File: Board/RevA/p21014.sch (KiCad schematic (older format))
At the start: 1 part

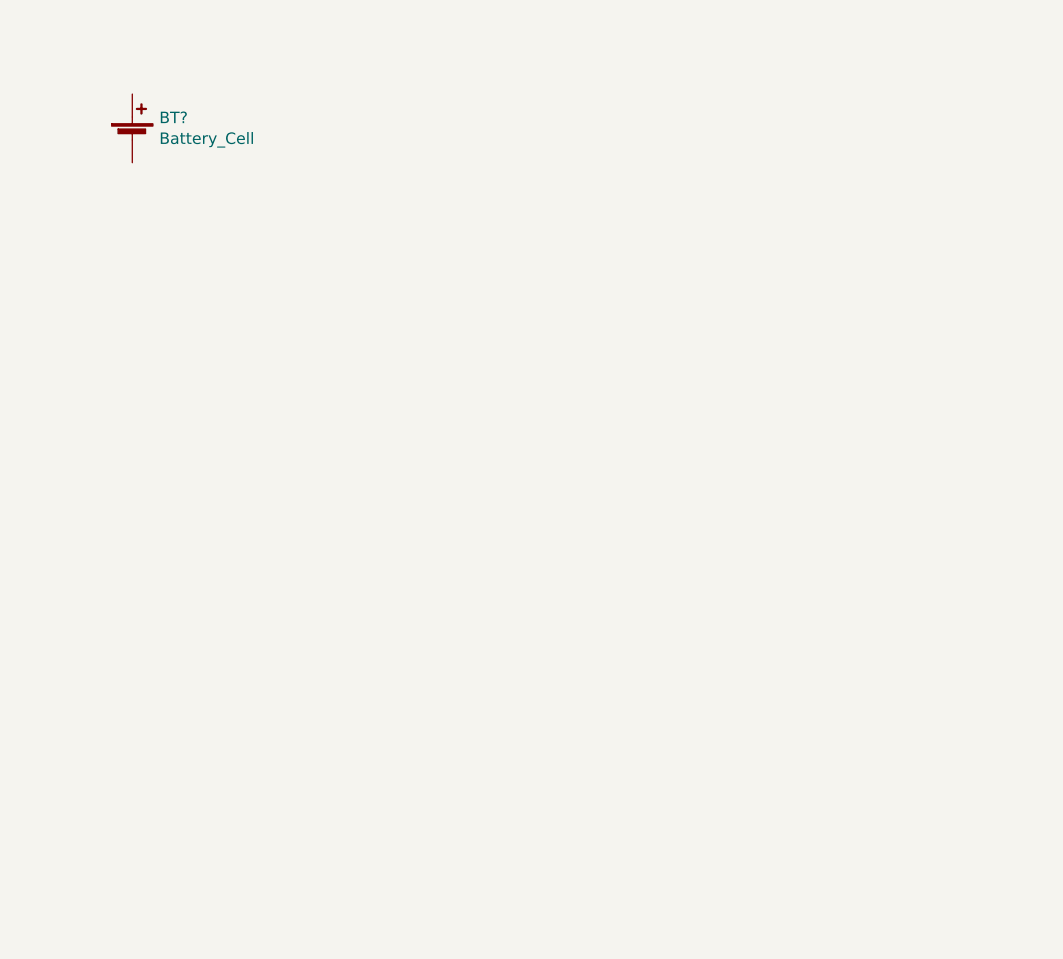
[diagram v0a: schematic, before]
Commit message: Added Initial Components to RevA Board
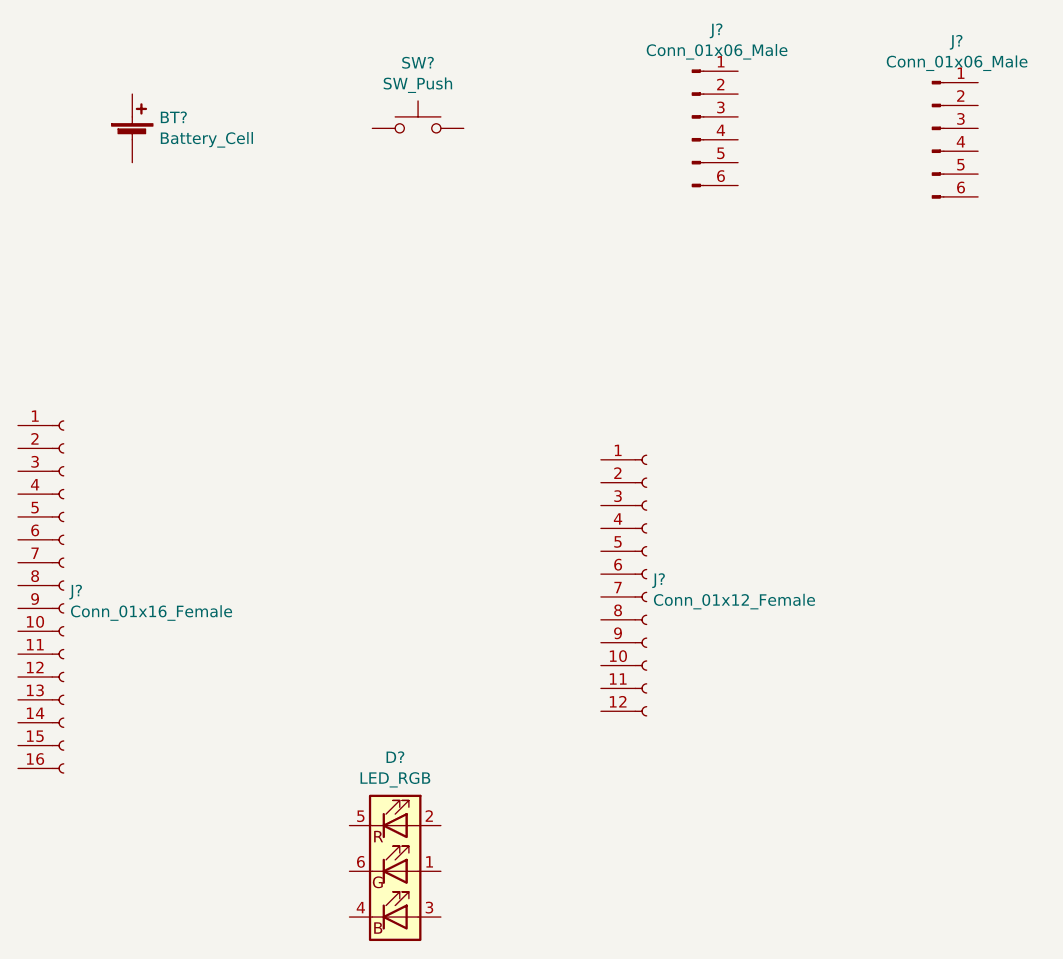
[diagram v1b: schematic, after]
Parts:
- added D?: LED_RGB, symbol AJS_Symbols:LED_RGB
- added J? (x2): Conn_01x06_Male, symbol Connector:Conn_01x06_Male
- added J?: Conn_01x16_Female, symbol Connector:Conn_01x16_Female
- added J?: Conn_01x12_Female, symbol Connector:Conn_01x12_Female
- added SW?: SW_Push, symbol Switch:SW_Push
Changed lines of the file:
@@
+	1    0    0    -1
+$EndComp
+$Comp
+L Switch:SW_Push SW?
+U 1 1 6149E8EA
+P 5050 1800
+F 0 "SW?" H 5050 2085 50  0000 C CNN
+F 1 "SW_Push" H 5050 1994 50  0000 C CNN
+F 2 "" H 5050 2000 50  0001 C CNN
+F 3 "~" H 5050 2000 50  0001 C CNN
+	1    5050 1800
+	1    0    0    -1
+$EndComp
+$Comp
+L Connector:Conn_01x06_Male J?
+U 1 1 6149F03E
+P 6250 1750
+F 0 "J?" H 6358 2131 50  0000 C CNN
+F 1 "Conn_01x06_Male" H 6358 2040 50  0000 C CNN
+F 2 "" H 6250 1750 50  0001 C CNN
+F 3 "~" H 6250 1750 50  0001 C CNN
+	1    6250 1750
+	1    0    0    -1
+$EndComp
+$Comp
+L Connector:Conn_01x06_Male J?
+U 1 1 6149FEAB
+P 7300 1800
+F 0 "J?" H 7408 2181 50  0000 C CNN
+F 1 "Conn_01x06_Male" H 7408 2090 50  0000 C CNN
+F 2 "" H 7300 1800 50  0001 C CNN
+F 3 "~" H 7300 1800 50  0001 C CNN
+	1    7300 1800
+	1    0    0    -1
+$EndComp
+$Comp
+L Connector:Conn_01x16_Female J?
+U 1 1 614A02F4
+P 3500 3800
+F 0 "J?" H 3528 3776 50  0000 L CNN
+F 1 "Conn_01x16_Female" H 3528 3685 50  0000 L CNN
+F 2 "" H 3500 3800 50  0001 C CNN
+F 3 "~" H 3500 3800 50  0001 C CNN
+	1    3500 3800
+	1    0    0    -1
+$EndComp
+$Comp
+L Connector:Conn_01x12_Female J?
+U 1 1 614A164B
+P 6050 3750
+F 0 "J?" H 6078 3726 50  0000 L CNN
+F 1 "Conn_01x12_Female" H 6078 3635 50  0000 L CNN
+F 2 "" H 6050 3750 50  0001 C CNN
+F 3 "~" H 6050 3750 50  0001 C CNN
+	1    6050 3750
+	1    0    0    -1
+$EndComp
+$Comp
+L AJS_Symbols:LED_RGB D?
+U 1 1 614AD0B3
+P 4950 5050
+F 0 "D?" H 4950 5547 50  0000 C CNN
+F 1 "LED_RGB" H 4950 5456 50  0000 C CNN
+F 2 "" H 4950 5000 50  0001 C CNN
+F 3 "~" H 4950 5000 50  0001 C CNN
+	1    4950 5050
 	1    0    0    -1
 $EndComp

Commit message: Restructure Board, Added Sheets and Layout to RevA
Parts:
- removed J? (x2): Conn_01x06_Male, symbol Connector:Conn_01x06_Male
- removed J?: Conn_01x16_Female, symbol Connector:Conn_01x16_Female
- removed J?: Conn_01x12_Female, symbol Connector:Conn_01x12_Female
- added D?: LED, symbol Device:LED
- added R?: R_US, symbol Device:R_US
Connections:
- net at BT?.1 (+): now also SW?.1
- net GNDREF: now reaches BT?.2 (-)
- net GNDREF: now also D?.1 (K)
- net +BATT: now reaches SW?.2
- net +BATT: now also R?.1
- new net: D?.2 (A), R?.2
- no-connect marks 0 -> 2
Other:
- moved on the sheet: SW?

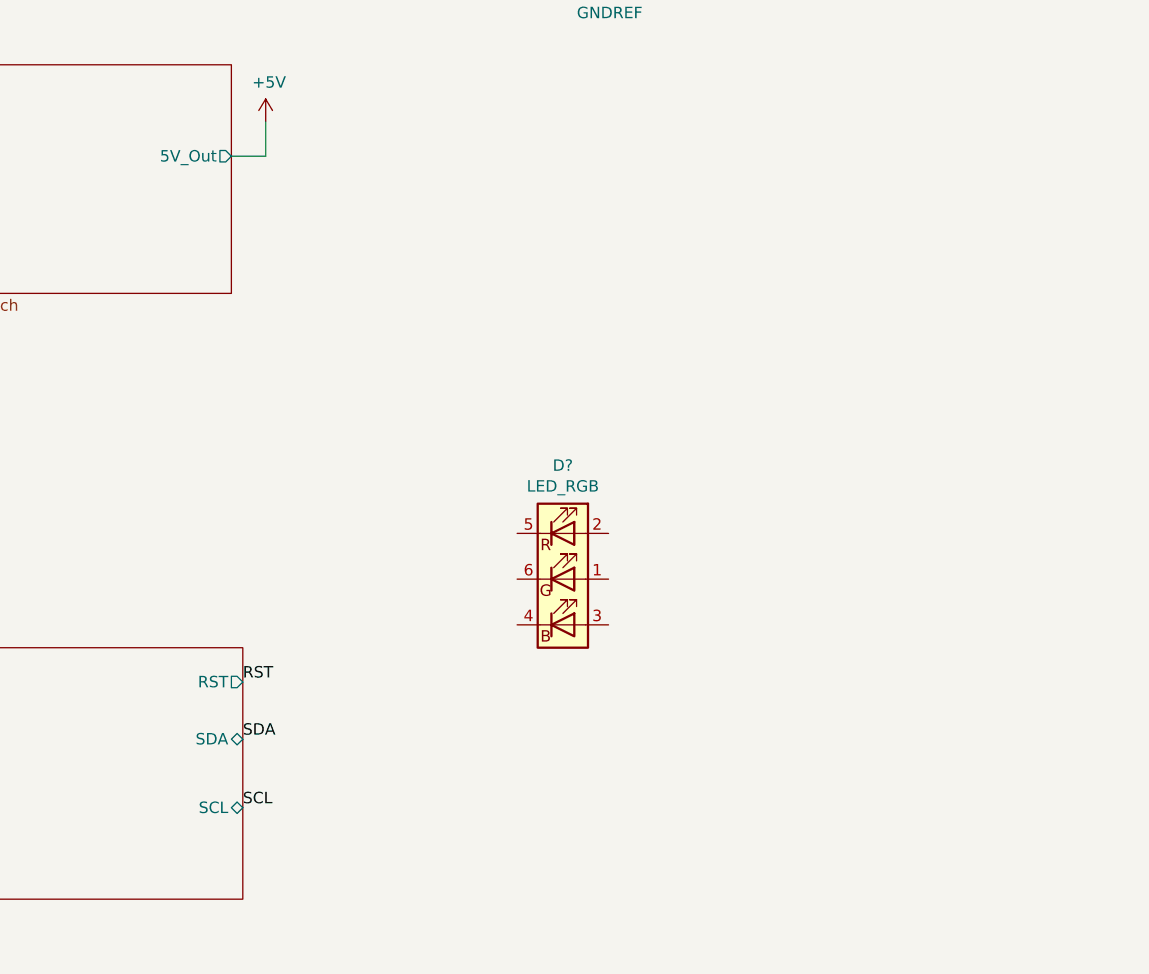
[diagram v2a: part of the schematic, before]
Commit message: Added Microcontroller Logic to RevA
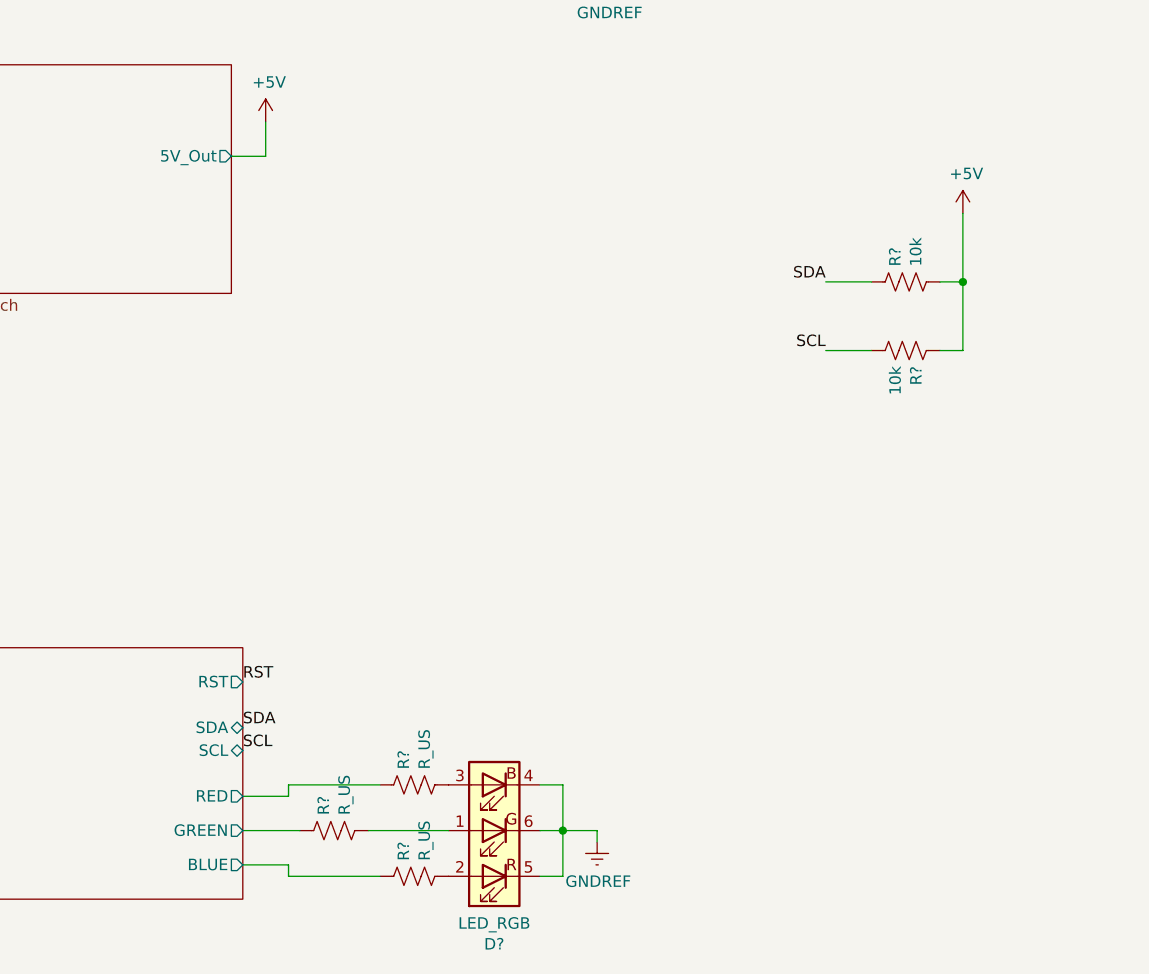
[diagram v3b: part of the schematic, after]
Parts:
- added R? (x2): 10k, symbol Device:R_US
- added R? (x3): R_US, symbol Device:R_US
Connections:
- net +5V: now also R?.1, R?.2
- net GNDREF: now also D?.4 (BK), D?.5 (RK), D?.6 (GK)
- net SCL: now also R?.2
- net SDA: now also R?.1
- net at D?.1 (GA): now also R?.2
- net at D?.2 (RA): now also R?.2
- net at D?.3 (BA): now also R?.2
- new net Feather_Board/BLUE: R?.1
- new net Feather_Board/GREEN: R?.1
- new net Feather_Board/RED: R?.1
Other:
- moved on the sheet: D?
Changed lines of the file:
@@
 F0 "Feather_Board" 50
 F1 "microcontroller.sch" 50
-F2 "SDA" B R 3550 5750 50
-F3 "SCL" B R 3550 6050 50
+F2 "SDA" B R 3550 5700 50
+F3 "SCL" B R 3550 5800 50
 F4 "5V_In" I L 1450 5700 50
 F5 "GND" I L 1450 6200 50
 F6 "RST" O R 3550 5500 50
+F7 "RED" O R 3550 6000 50
+F8 "GREEN" O R 3550 6150 50
+F9 "BLUE" O R 3550 6300 50
 $EndSheet
-$Comp
-L AJS_Symbols:LED_RGB D?
-U 1 1 614AD0B3
-P 4950 5050
-F 0 "D?" H 4950 5547 50  0000 C CNN
-F 1 "LED_RGB" H 4950 5456 50  0000 C CNN
-F 2 "" H 4950 5000 50  0001 C CNN
-F 3 "~" H 4950 5000 50  0001 C CNN
-	1    4950 5050
-	1    0    0    -1
-$EndComp
 $Comp
 L power:+5V #PWR?
@@
 Text Label 3550 5500 0    50   ~ 0
 RST
-Text Label 3550 5750 0    50   ~ 0
+Text Label 3550 5700 0    50   ~ 0
 SDA
-Text Label 3550 6050 0    50   ~ 0
+Text Label 3550 5800 0    50   ~ 0
 SCL
 $Comp
@@
 Wire Wire Line
 	3650 3200 3500 3200
+$Comp
+L power:+5V #PWR?
+U 1 1 614A01E3
+P 6700 3450
+F 0 "#PWR?" H 6700 3300 50  0001 C CNN
+F 1 "+5V" H 6715 3623 50  0000 C CNN
+F 2 "" H 6700 3450 50  0001 C CNN
+F 3 "" H 6700 3450 50  0001 C CNN
+	1    6700 3450
+	1    0    0    -1
+$EndComp
+$Comp
+L Device:R_US R?
+U 1 1 614A1141
+P 6450 3750
+F 0 "R?" H 6518 3796 50  0000 L CNN
+F 1 "10k" H 6518 3705 50  0000 L CNN
+F 2 "" V 6490 3740 50  0001 C CNN
+F 3 "~" H 6450 3750 50  0001 C CNN
+	1    6450 3750
+	0    -1   -1   0
+$EndComp
+Wire Wire Line
+	6600 3750 6700 3750
+Wire Wire Line
+	6700 3450 6700 3750
+Wire Wire Line
+	6700 3750 6700 4050
+Wire Wire Line
+	6700 4050 6600 4050
+Connection ~ 6700 3750
+$Comp
+L Device:R_US R?
+U 1 1 614A4AB2
+P 6450 4050
+F 0 "R?" H 6518 4096 50  0000 L CNN
+F 1 "10k" H 6518 4005 50  0000 L CNN
+F 2 "" V 6490 4040 50  0001 C CNN
+F 3 "~" H 6450 4050 50  0001 C CNN
+	1    6450 4050
+	0    1    1    0
+$EndComp
+Text Label 6100 4050 2    50   ~ 0
+SCL
+Text Label 6100 3750 2    50   ~ 0
+SDA
+Wire Wire Line
+	6100 3750 6300 3750
+Wire Wire Line
+	6300 4050 6100 4050
+$Comp
+L AJS_Symbols:LED_RGB D?
+U 1 1 614AD0B3
+P 4650 6150
+F 0 "D?" H 4650 6647 50  0000 C CNN
+F 1 "LED_RGB" H 4650 6556 50  0000 C CNN
+F 2 "" H 4650 6100 50  0001 C CNN
+F 3 "~" H 4650 6100 50  0001 C CNN
+	1    4650 6150
+	-1   0    0    1
+$EndComp
+Wire Wire Line
+	4850 5950 4950 5950
+Wire Wire Line
+	4950 5950 4950 6150
+Wire Wire Line
+	4950 6350 4850 6350
+Wire Wire Line
+	4850 6150 4950 6150
+Connection ~ 4950 6150
+Wire Wire Line
+	4950 6150 4950 6350
+$Comp
+L power:GNDREF #PWR?
+U 1 1 614BB4B2
+P 5100 6200
+F 0 "#PWR?" H 5100 5950 50  0001 C CNN
+F 1 "GNDREF" H 5105 6027 50  0000 C CNN
+F 2 "" H 5100 6200 50  0001 C CNN
+F 3 "" H 5100 6200 50  0001 C CNN
+	1    5100 6200
+	1    0    0    -1
+$EndComp
+Wire Wire Line
+	4950 6150 5100 6150
+Wire Wire Line
+	5100 6150 5100 6200
+$Comp
+L Device:R_US R?
+U 1 1 614BCF7D
+P 4300 5950
+F 0 "R?" H 4368 5996 50  0000 L CNN
+F 1 "R_US" H 4368 5905 50  0000 L CNN
+F 2 "" V 4340 5940 50  0001 C CNN
+F 3 "~" H 4300 5950 50  0001 C CNN
+	1    4300 5950
+	0    -1   -1   0
+$EndComp
+$Comp
+L Device:R_US R?
+U 1 1 614BE031
+P 3950 6150
+F 0 "R?" H 4018 6196 50  0000 L CNN
+F 1 "R_US" H 4018 6105 50  0000 L CNN
+F 2 "" V 3990 6140 50  0001 C CNN
+F 3 "~" H 3950 6150 50  0001 C CNN
+	1    3950 6150
+	0    -1   -1   0
+$EndComp
+$Comp
+L Device:R_US R?
+U 1 1 614BEAA2
+P 4300 6350
+F 0 "R?" H 4368 6396 50  0000 L CNN
+F 1 "R_US" H 4368 6305 50  0000 L CNN
+F 2 "" V 4340 6340 50  0001 C CNN
+F 3 "~" H 4300 6350 50  0001 C CNN
+	1    4300 6350
+	0    -1   -1   0
+$EndComp
+Wire Wire Line
+	4450 6150 4100 6150
+Wire Wire Line
+	3800 6150 3550 6150
+Wire Wire Line
+	3550 6000 3750 6000
+Wire Wire Line
+	3750 6000 3750 5950
+Wire Wire Line
+	3750 5950 4150 5950
+Wire Wire Line
+	4150 6350 3750 6350
+Wire Wire Line
+	3750 6350 3750 6300
+Wire Wire Line
+	3750 6300 3550 6300
 $EndSCHEMATC

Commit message: Finished Rough RevA and Added Annotations
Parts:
- R1, R2, R3, R4: renamed from R?; value R_US -> 350
- gave numbers to parts that had none: 6
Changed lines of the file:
@@
 $EndDescr
 $Comp
-L Device:Battery_Cell BT?
+L Device:Battery_Cell BT1
 U 1 1 6149E215
 P 3800 1850
-F 0 "BT?" H 3918 1946 50  0000 L CNN
+F 0 "BT1" H 3918 1946 50  0000 L CNN
 F 1 "Battery_Cell" H 3918 1855 50  0000 L CNN
 F 2 "" V 3800 1910 50  0001 C CNN
@@
 $EndComp
 $Comp
-L Switch:SW_Push SW?
+L Switch:SW_Push SW1
 U 1 1 6149E8EA
 P 4200 1450
-F 0 "SW?" H 4200 1735 50  0000 C CNN
+F 0 "SW1" H 4200 1735 50  0000 C CNN
 F 1 "SW_Push" H 4200 1644 50  0000 C CNN
 F 2 "" H 4200 1650 50  0001 C CNN
@@
 $EndSheet
 $Comp
-L power:GNDREF #PWR?
+L power:GNDREF #PWR0101
 U 1 1 614B1DB7
 P 7650 2300
-F 0 "#PWR?" H 7650 2050 50  0001 C CNN
+F 0 "#PWR0101" H 7650 2050 50  0001 C CNN
 F 1 "GNDREF" H 7655 2127 50  0000 C CNN
 F 2 "" H 7650 2300 50  0001 C CNN
@@
 $EndComp
 $Comp
-L power:GNDREF #PWR?
+L power:GNDREF #PWR0102
 U 1 1 614B3224
 P 7750 4450
-F 0 "#PWR?" H 7750 4200 50  0001 C CNN
+F 0 "#PWR0102" H 7750 4200 50  0001 C CNN
 F 1 "GNDREF" H 7755 4277 50  0000 C CNN
 F 2 "" H 7750 4450 50  0001 C CNN
@@
 	3800 1450 3800 1650
 $Comp
-L power:GNDREF #PWR?
+L power:GNDREF #PWR0103
 U 1 1 614B4CC5
 P 3800 2100
-F 0 "#PWR?" H 3800 1850 50  0001 C CNN
+F 0 "#PWR0103" H 3800 1850 50  0001 C CNN
 F 1 "GNDREF" H 3805 1927 50  0000 C CNN
 F 2 "" H 3800 2100 50  0001 C CNN
@@
 	3800 1950 3800 2100
 $Comp
-L power:+BATT #PWR?
+L power:+BATT #PWR0104
 U 1 1 614B51F6
 P 4650 1250
-F 0 "#PWR?" H 4650 1100 50  0001 C CNN
+F 0 "#PWR0104" H 4650 1100 50  0001 C CNN
 F 1 "+BATT" H 4665 1423 50  0000 C CNN
 F 2 "" H 4650 1250 50  0001 C CNN
@@
 $EndSheet
 $Comp
-L power:+5V #PWR?
+L power:+5V #PWR0105
 U 1 1 614B8AF7
 P 7800 1550
-F 0 "#PWR?" H 7800 1400 50  0001 C CNN
+F 0 "#PWR0105" H 7800 1400 50  0001 C CNN
 F 1 "+5V" H 7815 1723 50  0000 C CNN
 F 2 "" H 7800 1550 50  0001 C CNN
@@
 	7800 1700 8000 1700
 $Comp
-L power:+5V #PWR?
+L power:+5V #PWR0106
 U 1 1 614B9875
 P 7850 3650
-F 0 "#PWR?" H 7850 3500 50  0001 C CNN
+F 0 "#PWR0106" H 7850 3500 50  0001 C CNN
 F 1 "+5V" H 7865 3823 50  0000 C CNN
 F 2 "" H 7850 3650 50  0001 C CNN
@@
 $EndSheet
 $Comp
-L power:+BATT #PWR?
+L power:+BATT #PWR0107
 U 1 1 614BB053
 P 1550 2800
-F 0 "#PWR?" H 1550 2650 50  0001 C CNN
+F 0 "#PWR0107" H 1550 2650 50  0001 C CNN
 F 1 "+BATT" H 1565 2973 50  0000 C CNN
 F 2 "" H 1550 2800 50  0001 C CNN
@@
 	1550 2800 1550 3050
 $Comp
-L power:GNDREF #PWR?
+L power:GNDREF #PWR0108
 U 1 1 614BBAF0
 P 1600 3800
-F 0 "#PWR?" H 1600 3550 50  0001 C CNN
+F 0 "#PWR0108" H 1600 3550 50  0001 C CNN
 F 1 "GNDREF" H 1605 3627 50  0000 C CNN
 F 2 "" H 1600 3800 50  0001 C CNN
@@
 SCL
 $Comp
-L power:GNDREF #PWR?
+L power:GNDREF #PWR0109
 U 1 1 614BFC0D
 P 1100 6350
-F 0 "#PWR?" H 1100 6100 50  0001 C CNN
+F 0 "#PWR0109" H 1100 6100 50  0001 C CNN
 F 1 "GNDREF" H 1105 6177 50  0000 C CNN
 F 2 "" H 1100 6350 50  0001 C CNN
@@
 	1100 6200 1100 6350
 $Comp
-L power:+5V #PWR?
+L power:+5V #PWR0110
 U 1 1 614BFC15
 P 1250 5550
-F 0 "#PWR?" H 1250 5400 50  0001 C CNN
+F 0 "#PWR0110" H 1250 5400 50  0001 C CNN
 F 1 "+5V" H 1265 5723 50  0000 C CNN
 F 2 "" H 1250 5550 50  0001 C CNN
@@
 	1250 5700 1450 5700
 $Comp
-L Device:LED D?
+L Device:LED D2
 U 1 1 614C1039
 P 5150 2150
-F 0 "D?" V 5189 2032 50  0000 R CNN
+F 0 "D2" V 5189 2032 50  0000 R CNN
 F 1 "LED" V 5098 2032 50  0000 R CNN
 F 2 "" H 5150 2150 50  0001 C CNN
@@
 $EndComp
 $Comp
-L power:GNDREF #PWR?
+L power:GNDREF #PWR0111
 U 1 1 614C2D0B
 P 5150 2400
-F 0 "#PWR?" H 5150 2150 50  0001 C CNN
+F 0 "#PWR0111" H 5150 2150 50  0001 C CNN
 F 1 "GNDREF" H 5155 2227 50  0000 C CNN
 F 2 "" H 5150 2400 50  0001 C CNN
@@
 	5150 2300 5150 2400
 $Comp
-L Device:R_US R?
+L Device:R_US R4
 U 1 1 614C409D
 P 5150 1750
-F 0 "R?" H 5218 1796 50  0000 L CNN
-F 1 "R_US" H 5218 1705 50  0000 L CNN
+F 0 "R4" H 5218 1796 50  0000 L CNN
+F 1 "350" H 5218 1705 50  0000 L CNN
 F 2 "" V 5190 1740 50  0001 C CNN
 F 3 "~" H 5150 1750 50  0001 C CNN
@@
 Connection ~ 4650 1450
 $Comp
-L power:+5V #PWR?
+L power:+5V #PWR0112
 U 1 1 614C675A
 P 3650 3050
-F 0 "#PWR?" H 3650 2900 50  0001 C CNN
+F 0 "#PWR0112" H 3650 2900 50  0001 C CNN
 F 1 "+5V" H 3665 3223 50  0000 C CNN
 F 2 "" H 3650 3050 50  0001 C CNN
@@
 	3650 3200 3500 3200
 $Comp
-L power:+5V #PWR?
+L power:+5V #PWR0113
 U 1 1 614A01E3
 P 6700 3450
-F 0 "#PWR?" H 6700 3300 50  0001 C CNN
+F 0 "#PWR0113" H 6700 3300 50  0001 C CNN
 F 1 "+5V" H 6715 3623 50  0000 C CNN
 F 2 "" H 6700 3450 50  0001 C CNN
@@
 $EndComp
 $Comp
-L Device:R_US R?
+L Device:R_US R5
 U 1 1 614A1141
 P 6450 3750
-F 0 "R?" H 6518 3796 50  0000 L CNN
+F 0 "R5" H 6518 3796 50  0000 L CNN
 F 1 "10k" H 6518 3705 50  0000 L CNN
 F 2 "" V 6490 3740 50  0001 C CNN
@@
 Connection ~ 6700 3750
 $Comp
-L Device:R_US R?
+L Device:R_US R6
 U 1 1 614A4AB2
 P 6450 4050
-F 0 "R?" H 6518 4096 50  0000 L CNN
+F 0 "R6" H 6518 4096 50  0000 L CNN
 F 1 "10k" H 6518 4005 50  0000 L CNN
 F 2 "" V 6490 4040 50  0001 C CNN
@@
 	6300 4050 6100 4050
 $Comp
-L AJS_Symbols:LED_RGB D?
+L AJS_Symbols:LED_RGB D1
 U 1 1 614AD0B3
 P 4650 6150
-F 0 "D?" H 4650 6647 50  0000 C CNN
+F 0 "D1" H 4650 6647 50  0000 C CNN
 F 1 "LED_RGB" H 4650 6556 50  0000 C CNN
 F 2 "" H 4650 6100 50  0001 C CNN
@@
 	4950 6150 4950 6350
 $Comp
-L power:GNDREF #PWR?
+L power:GNDREF #PWR0114
 U 1 1 614BB4B2
 P 5100 6200
-F 0 "#PWR?" H 5100 5950 50  0001 C CNN
+F 0 "#PWR0114" H 5100 5950 50  0001 C CNN
 F 1 "GNDREF" H 5105 6027 50  0000 C CNN
 F 2 "" H 5100 6200 50  0001 C CNN
@@
 	5100 6150 5100 6200
 $Comp
-L Device:R_US R?
+L Device:R_US R2
 U 1 1 614BCF7D
 P 4300 5950
-F 0 "R?" H 4368 5996 50  0000 L CNN
-F 1 "R_US" H 4368 5905 50  0000 L CNN
+F 0 "R2" H 4368 5996 50  0000 L CNN
+F 1 "350" H 4368 5905 50  0000 L CNN
 F 2 "" V 4340 5940 50  0001 C CNN
 F 3 "~" H 4300 5950 50  0001 C CNN
@@
 $EndComp
 $Comp
-L Device:R_US R?
+L Device:R_US R1
 U 1 1 614BE031
 P 3950 6150
-F 0 "R?" H 4018 6196 50  0000 L CNN
-F 1 "R_US" H 4018 6105 50  0000 L CNN
+F 0 "R1" H 4018 6196 50  0000 L CNN
+F 1 "350" H 4018 6105 50  0000 L CNN
 F 2 "" V 3990 6140 50  0001 C CNN
 F 3 "~" H 3950 6150 50  0001 C CNN
@@
 $EndComp
 $Comp
-L Device:R_US R?
+L Device:R_US R3
 U 1 1 614BEAA2
 P 4300 6350
-F 0 "R?" H 4368 6396 50  0000 L CNN
-F 1 "R_US" H 4368 6305 50  0000 L CNN
+F 0 "R3" H 4368 6396 50  0000 L CNN
+F 1 "350" H 4368 6305 50  0000 L CNN
 F 2 "" V 4340 6340 50  0001 C CNN
 F 3 "~" H 4300 6350 50  0001 C CNN
